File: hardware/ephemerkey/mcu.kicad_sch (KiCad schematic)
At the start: 19 parts, among them J1 SWD TC2030-NL, J2 LOCK OUT, SW1 PROV/SHOW, U1 STM32U083KCU6, Y1 32.768kHz

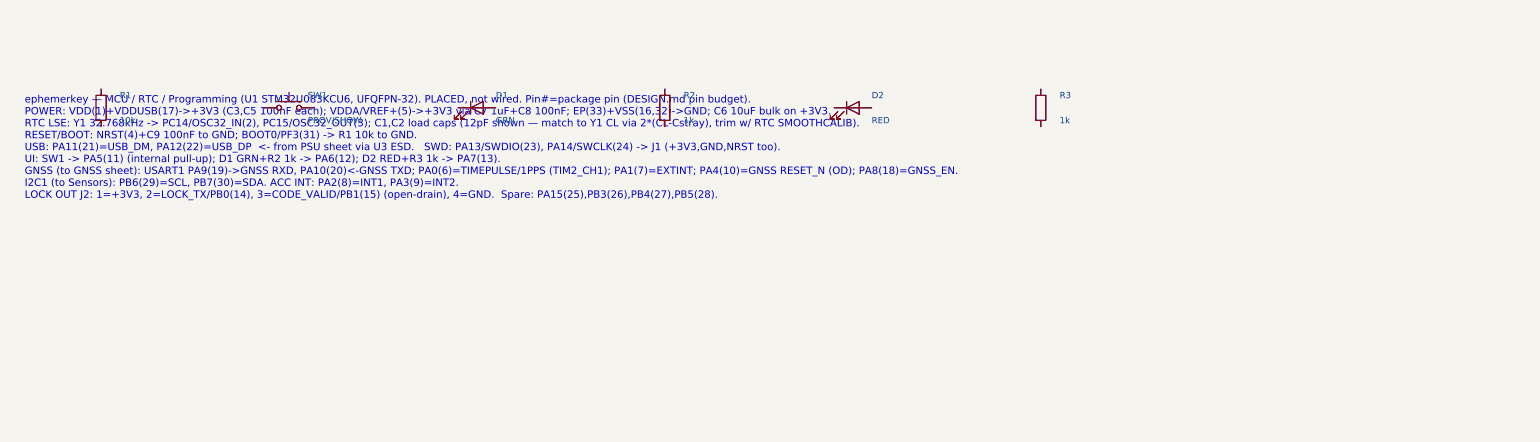
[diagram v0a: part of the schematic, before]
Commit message: Pinout-guide notes; vendor MAX + switch 3D models; 3 user buttons + DFU
Wiring notes: rewrote the four sheet notes from run-on prose into per-pin
PINOUT GUIDES (pin → net/function tables) per request.

3D models:
- MAX-M10S: vendored ublox_MAX-M10S.step (u-blox MAX form-factor, AP214, from
  fcmadwar/3D-Step-Models-Library) + project footprint ephemerkey:ublox_MAX
  with (model) repointed. Verify offset/rotation in 3D viewer.
- Switches: reuse tsumikoro's vendored ephemerkey:SW_Push_1P1T_XKB_TS-1187A
  footprint + STEP (the XKB TS-1187A model isn't in this KiCad bundle).
- Remaining to download: STM32U083 (UFQFPN-32), W3011A.

Switches: 3 user buttons (SW1→PA5, SW2→PA15 active-low; SW3→PF3/BOOT0
active-high). Holding SW3 at reset enters the STM32U0 ROM bootloader → USB DFU
over USB-C (confirmed in AN2606; crystal-less USB via HSI48+CRS).

make check: 59 components, 59/59 footprints, no dup refs. DESIGN.md pin budget +
library map, PARTS.md, 3dmodels README updated.

Co-Authored-By: Claude Opus 4.8 (1M context) <noreply@anthropic.com>
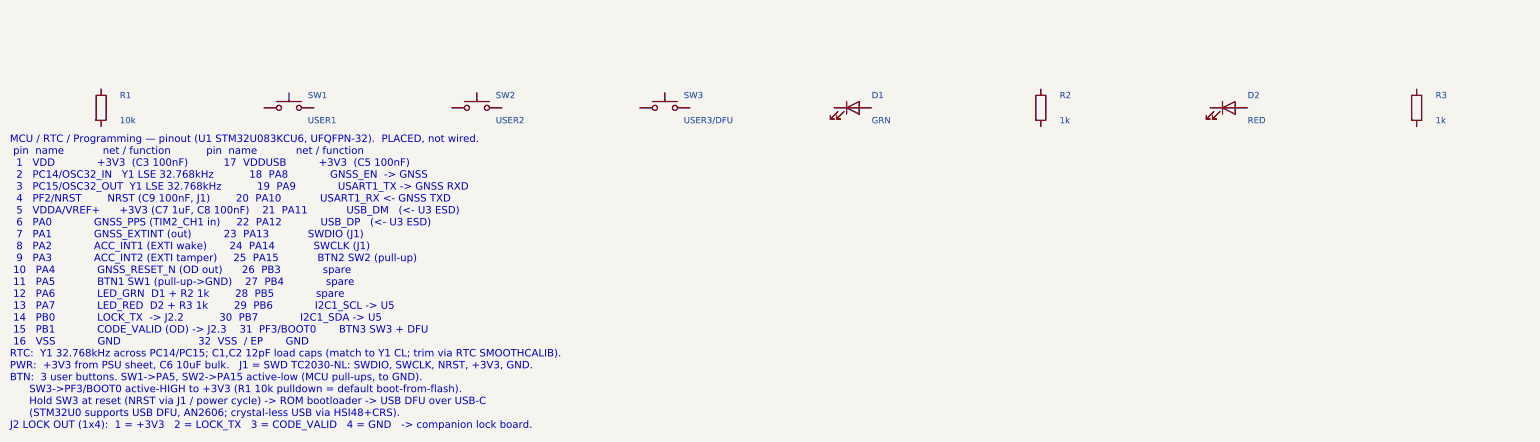
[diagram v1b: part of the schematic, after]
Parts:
- added SW2: USER2, ephemerkey:SW_Push_1P1T_XKB_TS-1187A, symbol Switch:SW_Push
- added SW3: USER3/DFU, ephemerkey:SW_Push_1P1T_XKB_TS-1187A, symbol Switch:SW_Push
- SW1: value PROV/SHOW -> USER1; footprint Button_Switch_SMD:SW_Push_1P1T_XKB_TS-1187A -> ephemerkey:SW_Push_1P1T_XKB_TS-1187A
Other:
- note added: "MCU / RTC / Programming — pinout (U1 STM32U083KCU6, UFQFPN-32). PLACED, not wired. pin name net / function pin name net / function 1 VDD +3V3 (C3 100nF) 17 VDDUSB +3V3 (C5 100nF) 2 PC14/OSC32_IN Y1 LSE 32.768kHz 18 PA8 GNSS_EN -> GNSS 3 PC15/OSC32_OUT Y1 LSE 32.768kHz 19 PA9 USART1_TX -> GNSS RXD 4 PF2/NRST NRST (C9 100nF, J1) 20 PA10 USART1_RX <- GNSS TXD 5 VDDA/VREF+ +3V3 (C7 1uF, C8 100nF) 21 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"
- note removed: "ephemerkey — MCU / RTC / Programming (U1 STM32U083KCU6, UFQFPN-32). PLACED, not wired. Pin#=package pin (DESIGN.md pin budget). POWER: VDD(1)+VDDUSB(17)->+3V3 (C3,C5 100nF each); VDDA/VREF+(5)->+3V3 via C7 1uF+C8 100nF; EP(33)+VSS(16,32)->GND; C6 10uF bulk on +3V3. RTC LSE: Y1 32.768kHz -> PC14/OSC32_IN(2), PC15/OSC32_OUT(3); C1,C2 load caps (12pF shown — match to Y1 CL via 2*(CL-Cstray), trim w/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"

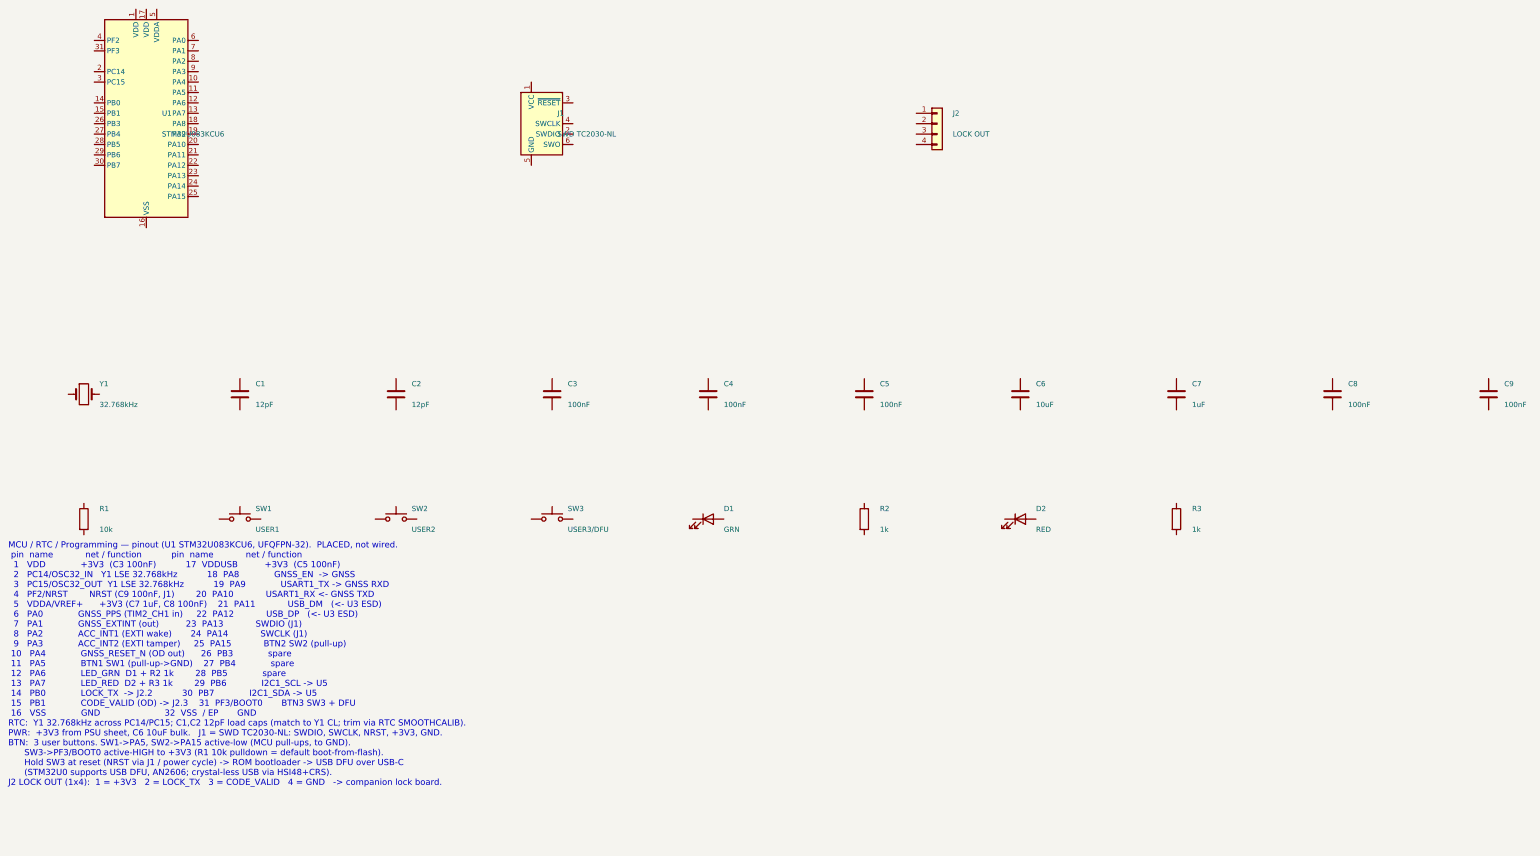
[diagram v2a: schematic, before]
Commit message: Add 128x32 I2C OLED (DS1) on a 4-pin 0.1" header
Uses the KiCad standard-library symbol Display_Graphic:ER_OLEDM0.91_1x-I2C
(0.91" = 128x32 I2C OLED panel type), mapped to a 4-pin 0.1" pin header
(PinHeader_1x04_P2.54mm_Vertical) so an OLED module plugs in.

Pinout: 1 GND, 2 VCC(3V3), 3 SCL->PB6, 4 SDA->PB7 — shares I2C1 with U5 LIS3DH
(OLED 0x3C vs LIS3DH 0x18); the existing R9/R10 4.7k pull-ups serve both.
Placed on the MCU sheet with the other connectors; renders correctly.

make check: 60 components, 60/60 footprints, no dup refs. DESIGN.md library
map + display open-question resolved; PARTS.md updated.

Co-Authored-By: Claude Opus 4.8 (1M context) <noreply@anthropic.com>
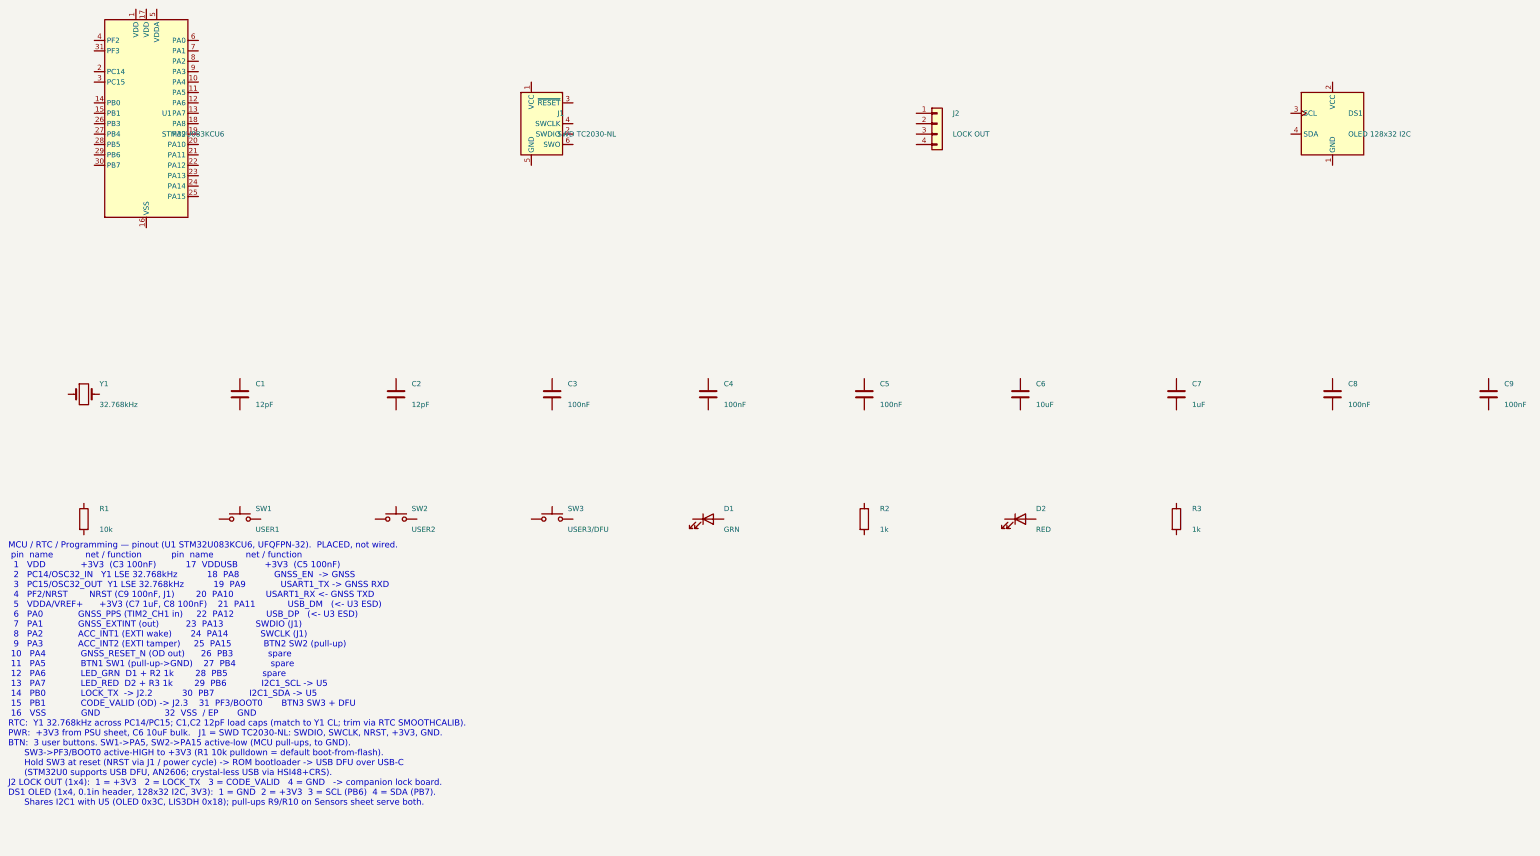
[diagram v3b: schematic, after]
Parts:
- added DS1: OLED 128x32 I2C, Connector_PinHeader_2.54mm:PinHeader_1x04_P2.54mm_Vertical, symbol Display_Graphic:ER_OLEDM0.91_1x-I2C

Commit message: OLED DS1: use female socket footprint (PinSocket_1x04_P2.54mm)
Per request, the 128x32 I2C OLED mounts in a 4-pin 0.1in female socket
(Connector_PinSocket_2.54mm:PinSocket_1x04_P2.54mm_Vertical, has a 3D model)
so the male-headered OLED module plugs in. DESIGN.md + PARTS.md updated.

Co-Authored-By: Claude Opus 4.8 (1M context) <noreply@anthropic.com>
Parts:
- DS1: footprint Connector_PinHeader_2.54mm:PinHeader_1x04_P2.54mm_Vertical -> Connector_PinSocket_2.54mm:PinSocket_1x04_P2.54mm_Vertical
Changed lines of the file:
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@@
 		(instances
 			(project "ephemerkey"
-				(path "/e1000000-0000-4000-8000-000000000001/3c8d3540-f809-4f1b-b1a4-022df44b5c09"
+				(path "/e1000000-0000-4000-8000-000000000001/8f68bf2c-35b7-40f9-b8ab-785f56914c2e"
 					(reference "U1")
 					(unit 1)
@@
 		(instances
 			(project "ephemerkey"
-				(path "/e1000000-0000-4000-8000-000000000001/3c8d3540-f809-4f1b-b1a4-022df44b5c09"
+				(path "/e1000000-0000-4000-8000-000000000001/8f68bf2c-35b7-40f9-b8ab-785f56914c2e"
 					(reference "J1")
 					(unit 1)
@@
 		(instances
 			(project "ephemerkey"
-				(path "/e1000000-0000-4000-8000-000000000001/3c8d3540-f809-4f1b-b1a4-022df44b5c09"
+				(path "/e1000000-0000-4000-8000-000000000001/8f68bf2c-35b7-40f9-b8ab-785f56914c2e"
 					(reference "J2")
 					(unit 1)
@@
 			(effects (font (size 1.27 1.27)) (justify left))
 		)
-		(property "Footprint" "Connector_PinHeader_2.54mm:PinHeader_1x04_P2.54mm_Vertical"
+		(property "Footprint" "Connector_PinSocket_2.54mm:PinSocket_1x04_P2.54mm_Vertical"
 			(at 335.2800 55.8800 0)
 			(effects (font (size 1.27 1.27))) (hide yes)
@@
 		(instances
 			(project "ephemerkey"
-				(path "/e1000000-0000-4000-8000-000000000001/3c8d3540-f809-4f1b-b1a4-022df44b5c09"
+				(path "/e1000000-0000-4000-8000-000000000001/8f68bf2c-35b7-40f9-b8ab-785f56914c2e"
 					(reference "DS1")
 					(unit 1)
@@
 		(instances
 			(project "ephemerkey"
-				(path "/e1000000-0000-4000-8000-000000000001/3c8d3540-f809-4f1b-b1a4-022df44b5c09"
+				(path "/e1000000-0000-4000-8000-000000000001/8f68bf2c-35b7-40f9-b8ab-785f56914c2e"
 					(reference "Y1")
 					(unit 1)
@@
 		(instances
 			(project "ephemerkey"
-				(path "/e1000000-0000-4000-8000-000000000001/3c8d3540-f809-4f1b-b1a4-022df44b5c09"
+				(path "/e1000000-0000-4000-8000-000000000001/8f68bf2c-35b7-40f9-b8ab-785f56914c2e"
 					(reference "C1")
 					(unit 1)
@@
 		(instances
 			(project "ephemerkey"
-				(path "/e1000000-0000-4000-8000-000000000001/3c8d3540-f809-4f1b-b1a4-022df44b5c09"
+				(path "/e1000000-0000-4000-8000-000000000001/8f68bf2c-35b7-40f9-b8ab-785f56914c2e"
 					(reference "C2")
 					(unit 1)
@@
 		(instances
 			(project "ephemerkey"
-				(path "/e1000000-0000-4000-8000-000000000001/3c8d3540-f809-4f1b-b1a4-022df44b5c09"
+				(path "/e1000000-0000-4000-8000-000000000001/8f68bf2c-35b7-40f9-b8ab-785f56914c2e"
 					(reference "C3")
 					(unit 1)
@@
 		(instances
 			(project "ephemerkey"
-				(path "/e1000000-0000-4000-8000-000000000001/3c8d3540-f809-4f1b-b1a4-022df44b5c09"
+				(path "/e1000000-0000-4000-8000-000000000001/8f68bf2c-35b7-40f9-b8ab-785f56914c2e"
 					(reference "C4")
 					(unit 1)
@@
 		(instances
 			(project "ephemerkey"
-				(path "/e1000000-0000-4000-8000-000000000001/3c8d3540-f809-4f1b-b1a4-022df44b5c09"
+				(path "/e1000000-0000-4000-8000-000000000001/8f68bf2c-35b7-40f9-b8ab-785f56914c2e"
 					(reference "C5")
 					(unit 1)
@@
 		(instances
 			(project "ephemerkey"
-				(path "/e1000000-0000-4000-8000-000000000001/3c8d3540-f809-4f1b-b1a4-022df44b5c09"
+				(path "/e1000000-0000-4000-8000-000000000001/8f68bf2c-35b7-40f9-b8ab-785f56914c2e"
 					(reference "C6")
 					(unit 1)
@@
 		(instances
 			(project "ephemerkey"
-				(path "/e1000000-0000-4000-8000-000000000001/3c8d3540-f809-4f1b-b1a4-022df44b5c09"
+				(path "/e1000000-0000-4000-8000-000000000001/8f68bf2c-35b7-40f9-b8ab-785f56914c2e"
 					(reference "C7")
 					(unit 1)
@@
 		(instances
 			(project "ephemerkey"
-				(path "/e1000000-0000-4000-8000-000000000001/3c8d3540-f809-4f1b-b1a4-022df44b5c09"
+				(path "/e1000000-0000-4000-8000-000000000001/8f68bf2c-35b7-40f9-b8ab-785f56914c2e"
 					(reference "C8")
 					(unit 1)
@@
 		(instances
 			(project "ephemerkey"
-				(path "/e1000000-0000-4000-8000-000000000001/3c8d3540-f809-4f1b-b1a4-022df44b5c09"
+				(path "/e1000000-0000-4000-8000-000000000001/8f68bf2c-35b7-40f9-b8ab-785f56914c2e"
 					(reference "C9")
 					(unit 1)
@@
 		(instances
 			(project "ephemerkey"
-				(path "/e1000000-0000-4000-8000-000000000001/3c8d3540-f809-4f1b-b1a4-022df44b5c09"
+				(path "/e1000000-0000-4000-8000-000000000001/8f68bf2c-35b7-40f9-b8ab-785f56914c2e"
 					(reference "R1")
 					(unit 1)
@@
 		(instances
 			(project "ephemerkey"
-				(path "/e1000000-0000-4000-8000-000000000001/3c8d3540-f809-4f1b-b1a4-022df44b5c09"
+				(path "/e1000000-0000-4000-8000-000000000001/8f68bf2c-35b7-40f9-b8ab-785f56914c2e"
 					(reference "SW1")
 					(unit 1)
@@
 		(instances
 			(project "ephemerkey"
-				(path "/e1000000-0000-4000-8000-000000000001/3c8d3540-f809-4f1b-b1a4-022df44b5c09"
+				(path "/e1000000-0000-4000-8000-000000000001/8f68bf2c-35b7-40f9-b8ab-785f56914c2e"
 					(reference "SW2")
 					(unit 1)
@@
 		(instances
 			(project "ephemerkey"
-				(path "/e1000000-0000-4000-8000-000000000001/3c8d3540-f809-4f1b-b1a4-022df44b5c09"
+				(path "/e1000000-0000-4000-8000-000000000001/8f68bf2c-35b7-40f9-b8ab-785f56914c2e"
 					(reference "SW3")
 					(unit 1)
@@
 		(instances
 			(project "ephemerkey"
-				(path "/e1000000-0000-4000-8000-000000000001/3c8d3540-f809-4f1b-b1a4-022df44b5c09"
+				(path "/e1000000-0000-4000-8000-000000000001/8f68bf2c-35b7-40f9-b8ab-785f56914c2e"
 					(reference "D1")
 					(unit 1)
@@
 		(instances
 			(project "ephemerkey"
-				(path "/e1000000-0000-4000-8000-000000000001/3c8d3540-f809-4f1b-b1a4-022df44b5c09"
+				(path "/e1000000-0000-4000-8000-000000000001/8f68bf2c-35b7-40f9-b8ab-785f56914c2e"
 					(reference "R2")
 					(unit 1)
@@
 		(instances
 			(project "ephemerkey"
-				(path "/e1000000-0000-4000-8000-000000000001/3c8d3540-f809-4f1b-b1a4-022df44b5c09"
+				(path "/e1000000-0000-4000-8000-000000000001/8f68bf2c-35b7-40f9-b8ab-785f56914c2e"
 					(reference "D2")
 					(unit 1)
@@
 		(instances
 			(project "ephemerkey"
-				(path "/e1000000-0000-4000-8000-000000000001/3c8d3540-f809-4f1b-b1a4-022df44b5c09"
+				(path "/e1000000-0000-4000-8000-000000000001/8f68bf2c-35b7-40f9-b8ab-785f56914c2e"
 					(reference "R3")
 					(unit 1)
